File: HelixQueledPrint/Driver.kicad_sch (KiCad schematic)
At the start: 7 parts, among them U202 TPS92201

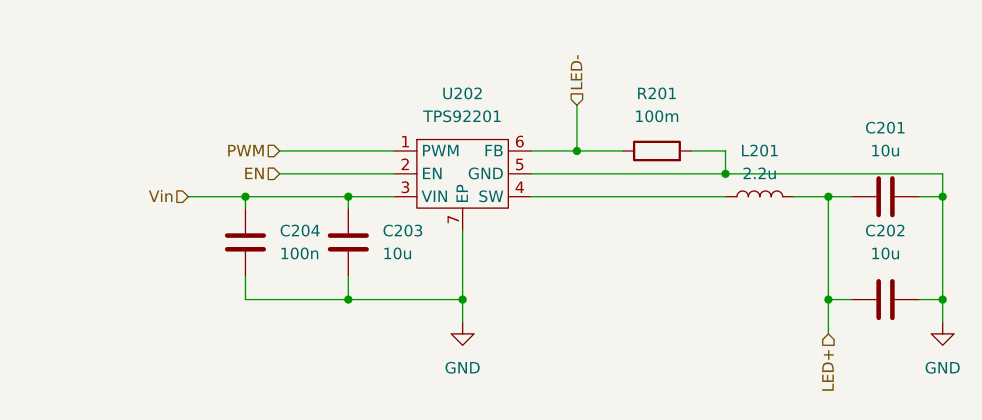
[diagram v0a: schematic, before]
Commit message: 5V Voeding toegevoegd
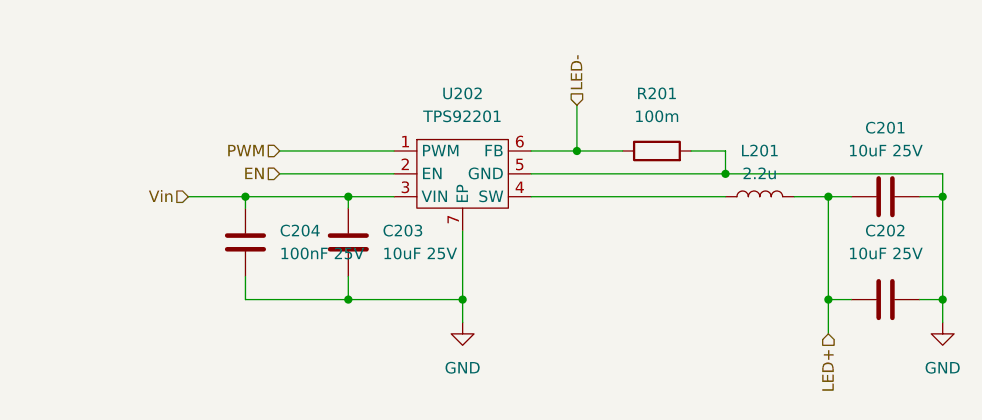
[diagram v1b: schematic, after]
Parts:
- C201, C202, C203: value 10u -> 10uF 25V; footprint (none) -> Capacitor_SMD:C_0805_2012Metric
- C204: value 100n -> 100nF 25V; footprint (none) -> Capacitor_SMD:C_0402_1005Metric
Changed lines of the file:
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@@
 			)
 		)
-		(property "Value" "10u"
+		(property "Value" "10uF 25V"
 			(at 123.19 88.8999 0)
 			(effects
@@
 			)
 		)
-		(property "Footprint" ""
+		(property "Footprint" "Capacitor_SMD:C_0805_2012Metric"
 			(at 118.4148 83.82 0)
 			(effects
@@
 			)
 		)
-		(property "Value" "10u"
+		(property "Value" "10uF 25V"
 			(at 179.07 88.9 90)
 			(effects
@@
 			)
 		)
-		(property "Footprint" ""
+		(property "Footprint" "Capacitor_SMD:C_0805_2012Metric"
 			(at 182.88 93.0148 0)
 			(effects
@@
 			)
 		)
-		(property "Value" "10u"
+		(property "Value" "10uF 25V"
 			(at 179.07 77.47 90)
 			(effects
@@
 			)
 		)
-		(property "Footprint" ""
+		(property "Footprint" "Capacitor_SMD:C_0805_2012Metric"
 			(at 182.88 81.5848 0)
 			(effects
@@
 			)
 		)
-		(property "Value" "100n"
+		(property "Value" "100nF 25V"
 			(at 111.76 88.8999 0)
 			(effects
@@
 			)
 		)
-		(property "Footprint" ""
+		(property "Footprint" "Capacitor_SMD:C_0402_1005Metric"
 			(at 106.9848 83.82 0)
 			(effects

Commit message: 3.3V voeding toegevoegd
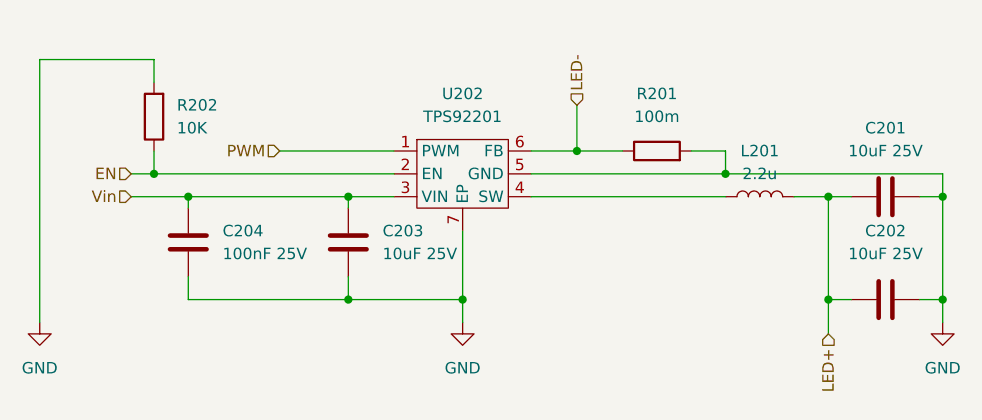
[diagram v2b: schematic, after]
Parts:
- added R202: 10K, symbol Device:R
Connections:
- net EN: now also R202.1
- net GND: now also R202.2
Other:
- moved on the sheet: C204
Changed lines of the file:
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@@
 	)
 	(junction
-		(at 107.95 82.55)
+		(at 97.79 80.01)
 		(diameter 0)
 		(color 0 0 0 0)
@@
 	)
 	(junction
+		(at 101.6 82.55)
+		(diameter 0)
+		(color 0 0 0 0)
+	)
+	(junction
 		(at 172.72 82.55)
 		(diameter 0)
@@
 	(wire
 		(pts
+			(xy 101.6 82.55) (xy 119.38 82.55)
+		)
+		(stroke
+			(width 0)
+			(type default)
+		)
+	)
+	(wire
+		(pts
 			(xy 185.42 93.98) (xy 185.42 82.55)
 		)
@@
 	(wire
 		(pts
-			(xy 107.95 82.55) (xy 119.38 82.55)
+			(xy 97.79 69.85) (xy 97.79 67.31)
+		)
+		(stroke
+			(width 0)
+			(type default)
+		)
+	)
+	(wire
+		(pts
+			(xy 97.79 80.01) (xy 124.46 80.01)
 		)
 		(stroke
@@
 	(wire
 		(pts
+			(xy 97.79 77.47) (xy 97.79 80.01)
+		)
+		(stroke
+			(width 0)
+			(type default)
+		)
+	)
+	(wire
+		(pts
 			(xy 139.7 82.55) (xy 161.29 82.55)
 		)
@@
 	(wire
 		(pts
-			(xy 107.95 93.98) (xy 119.38 93.98)
+			(xy 101.6 93.98) (xy 119.38 93.98)
+		)
+		(stroke
+			(width 0)
+			(type default)
+		)
+	)
+	(wire
+		(pts
+			(xy 85.09 67.31) (xy 85.09 96.52)
 		)
 		(stroke
@@
 	(wire
 		(pts
-			(xy 107.95 82.55) (xy 107.95 83.82)
+			(xy 101.6 82.55) (xy 101.6 83.82)
 		)
 		(stroke
@@
 	(wire
 		(pts
-			(xy 107.95 91.44) (xy 107.95 93.98)
+			(xy 101.6 91.44) (xy 101.6 93.98)
 		)
 		(stroke
@@
 	(wire
 		(pts
+			(xy 97.79 67.31) (xy 85.09 67.31)
+		)
+		(stroke
+			(width 0)
+			(type default)
+		)
+	)
+	(wire
+		(pts
 			(xy 161.29 80.01) (xy 185.42 80.01)
 		)
@@
 	(wire
 		(pts
-			(xy 111.76 80.01) (xy 124.46 80.01)
-		)
-		(stroke
-			(width 0)
-			(type default)
-		)
-	)
-	(wire
-		(pts
-			(xy 101.6 82.55) (xy 107.95 82.55)
+			(xy 95.25 80.01) (xy 97.79 80.01)
+		)
+		(stroke
+			(width 0)
+			(type default)
+		)
+	)
+	(wire
+		(pts
+			(xy 95.25 82.55) (xy 101.6 82.55)
 		)
 		(stroke
@@
 	(hierarchical_label "Vin"
 		(shape input)
-		(at 101.6 82.55 180)
+		(at 95.25 82.55 180)
 		(effects
 			(font
@@
 	(hierarchical_label "EN"
 		(shape input)
-		(at 111.76 80.01 180)
+		(at 95.25 80.01 180)
 		(effects
 			(font
@@
 	)
 	(symbol
+		(lib_id "Device:R")
+		(at 97.79 73.66 180)
+		(unit 1)
+		(exclude_from_sim no)
+		(in_bom yes)
+		(on_board yes)
+		(dnp no)
+		(fields_autoplaced yes)
+		(property "Reference" "R202"
+			(at 100.33 72.3899 0)
+			(effects
+				(font
+					(size 1.27 1.27)
+				)
+				(justify right)
+			)
+		)
+		(property "Value" "10K"
+			(at 100.33 74.9299 0)
+			(effects
+				(font
+					(size 1.27 1.27)
+				)
+				(justify right)
+			)
+		)
+		(property "Footprint" ""
+			(at 99.568 73.66 90)
+			(effects
+				(font
+					(size 1.27 1.27)
+				)
+				(hide yes)
+			)
+		)
+		(property "Datasheet" "~"
+			(at 97.79 73.66 0)
+			(effects
+				(font
+					(size 1.27 1.27)
+				)
+				(hide yes)
+			)
+		)
+		(property "Description" "Resistor"
+			(at 97.79 73.66 0)
+			(effects
+				(font
+					(size 1.27 1.27)
+				)
+				(hide yes)
+			)
+		)
+		(pin "1"
+		)
+		(pin "2"
+		)
+		(instances
+			(project "HelixQueledPrint"
+				(path "/398fd733-417c-46a8-b62a-83839861ebca/0e29c95a-1407-48f3-b8b9-9ad0be3fc14a"
+					(reference "R202")
+					(unit 1)
+				)
+				(path "/398fd733-417c-46a8-b62a-83839861ebca/4ec5e2f4-8826-4ee1-868c-24835ef0ed6d"
+					(reference "R402")
+					(unit 1)
+				)
+				(path "/398fd733-417c-46a8-b62a-83839861ebca/d0a2a03c-f7e4-4c8d-96d9-e0ad8b55bb56"
+					(reference "R502")
+					(unit 1)
+				)
+				(path "/398fd733-417c-46a8-b62a-83839861ebca/ea63bd13-3794-478b-8763-58324a67908c"
+					(reference "R302")
+					(unit 1)
+				)
+			)
+		)
+	)
+	(symbol
+		(lib_id "power:GND")
+		(at 85.09 96.52 0)
+		(unit 1)
+		(exclude_from_sim no)
+		(in_bom yes)
+		(on_board yes)
+		(dnp no)
+		(fields_autoplaced yes)
+		(property "Reference" "#PWR0203"
+			(at 85.09 102.87 0)
+			(effects
+				(font
+					(size 1.27 1.27)
+				)
+				(hide yes)
+			)
+		)
+		(property "Value" "GND"
+			(at 85.09 101.6 0)
+			(effects
+				(font
+					(size 1.27 1.27)
+				)
+			)
+		)
+		(property "Footprint" ""
+			(at 85.09 96.52 0)
+			(effects
+				(font
+					(size 1.27 1.27)
+				)
+				(hide yes)
+			)
+		)
+		(property "Datasheet" ""
+			(at 85.09 96.52 0)
+			(effects
+				(font
+					(size 1.27 1.27)
+				)
+				(hide yes)
+			)
+		)
+		(property "Description" "Power symbol creates a global label with name \"GND\" , ground"
+			(at 85.09 96.52 0)
+			(effects
+				(font
+					(size 1.27 1.27)
+				)
+				(hide yes)
+			)
+		)
+		(pin "1"
+		)
+		(instances
+			(project "HelixQueledPrint"
+				(path "/398fd733-417c-46a8-b62a-83839861ebca/0e29c95a-1407-48f3-b8b9-9ad0be3fc14a"
+					(reference "#PWR0203")
+					(unit 1)
+				)
+				(path "/398fd733-417c-46a8-b62a-83839861ebca/4ec5e2f4-8826-4ee1-868c-24835ef0ed6d"
+					(reference "#PWR0403")
+					(unit 1)
+				)
+				(path "/398fd733-417c-46a8-b62a-83839861ebca/d0a2a03c-f7e4-4c8d-96d9-e0ad8b55bb56"
+					(reference "#PWR0503")
+					(unit 1)
+				)
+				(path "/398fd733-417c-46a8-b62a-83839861ebca/ea63bd13-3794-478b-8763-58324a67908c"
+					(reference "#PWR0303")
+					(unit 1)
+				)
+			)
+		)
+	)
+	(symbol
 		(lib_id "power:GND")
 		(at 132.08 96.52 0)
@@
 	(symbol
 		(lib_id "Device:C")
-		(at 107.95 87.63 180)
+		(at 101.6 87.63 180)
 		(unit 1)
 		(exclude_from_sim no)
@@
 		(fields_autoplaced yes)
 		(property "Reference" "C204"
-			(at 111.76 86.3599 0)
+			(at 105.41 86.3599 0)
 			(effects
 				(font
@@
 		)
 		(property "Value" "100nF 25V"
-			(at 111.76 88.8999 0)
+			(at 105.41 88.8999 0)
 			(effects
 				(font
@@
 		)
 		(property "Footprint" "Capacitor_SMD:C_0402_1005Metric"
-			(at 106.9848 83.82 0)
+			(at 100.6348 83.82 0)
 			(effects
 				(font
@@
 		)
 		(property "Datasheet" "~"
-			(at 107.95 87.63 0)
+			(at 101.6 87.63 0)
 			(effects
 				(font
@@
 		)
 		(property "Description" "Unpolarized capacitor"
-			(at 107.95 87.63 0)
-			(effects
-				(font
+			(at 101.6 87.63 0)
+			(effects
+				(font

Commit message: footprints toegewezen
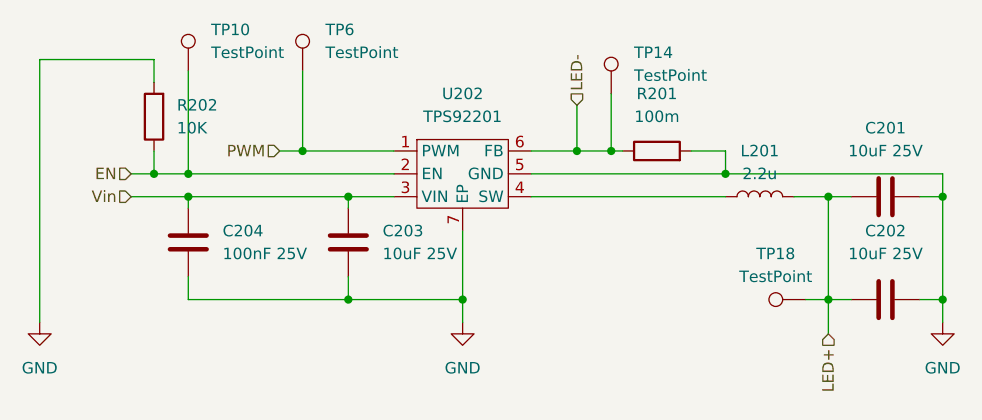
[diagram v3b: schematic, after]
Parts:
- added TP10, TP14, TP18, TP6: TestPoint, TestPoint:TestPoint_Pad_D1.0mm, symbol Connector:TestPoint
- L201: footprint (none) -> Inductor_SMD:L_APV_ANR4020; MPN (none) -> SMNR4020-2.2UH
- R201, R202: footprint (none) -> Resistor_SMD:R_0402_1005Metric
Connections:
- net EN: now also TP10.1
- net LED+: now also TP18.1
- net LED-: now also TP14.1
- net PWM: now also TP6.1
